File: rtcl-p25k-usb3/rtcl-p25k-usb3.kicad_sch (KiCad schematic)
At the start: 90 parts, among them J1 USB3_B_Micro, J10 SSQ-106-02-F-D-RA, J2 RASPPICAM22, J3 BTB-DF40C-60DS-0.4V(51), J4 BTB-DF40C-60DS-0.4V(51), J5 JTAG, U1 FT601Q, U12 TPS22917DBV, U2 TPD4E05U06DQA, U3 USBLC6-2P6, X1 30MHz

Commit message: Add new footprints for RES_YC104_YAG and RES_YC164_3P2X1P6_YAG
- Created footprint for RES_YC104_YAG with detailed properties and pads.
- Created footprint for RES_YC164_3P2X1P6_YAG with comprehensive design elements and specifications.
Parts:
- removed D1: PTVS5V0Z1USKP, Diode_SMD:Nexperia_DSN1608-2_1.6x0.8mm, symbol Diode:PTVS5V0Z1USKP
- removed L1: BLM18PG221SN1D, Resistor_SMD:R_0402_1005Metric, symbol Device:L
- removed R55: 0, Resistor_SMD:R_0402_1005Metric, symbol Device:R
- added C15: 0.1uF, Capacitor_SMD:C_0603_1608Metric, symbol Device:C
- added FB1: BLM18SG121TN1, symbol Device:FerriteBead
- added R59: 1M, Resistor_SMD:R_0402_1005Metric, symbol Device:R
- added RN2: YC104-JR-0722RL, rtcl-p25k-usb3:RES_YC104_YAG, symbol Device:R_Pack04
- added RN3: YC124-JR-1322RL, rtcl-p25k-usb3:RES_YC164_3P2X1P6_YAG, symbol Device:R_Pack04
- J1: value USB3_B_Micro -> ZX360D-B-10P(30); footprint (none) -> rtcl-p25k-usb3:CONN10_ZX360D-B-10P30_HIR; LCSC (none) -> C598201
- J2: footprint RASPPICAM22 -> (none)
- RN1: value R_Pack04 -> YC164-JR-0722RL; footprint Resistor_SMD:R_Array_Convex_4x0603 -> rtcl-p25k-usb3:RES_YC164_3P2X1P6_YAG
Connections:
- net +5V: now also FB1.2; no longer C10.2, J1.1 (VBUS), U1.37 (VBUS), U3.5 (VBUS)
- net FT601_BE0: now also RN2.4 (R4.1); no longer RN1.5 (R4.2)
- net FT601_BE1: now also RN2.3 (R3.1); no longer RN1.6 (R3.2)
- net FT601_BE2: now also RN2.2 (R2.1); no longer RN1.7 (R2.2)
- net FT601_BE3: now also RN2.1 (R1.1); no longer RN1.8 (R1.2)
- net GND: now also J1.8 (DRAIN), C15.1, R59.2
- net USB_SSRXM: now also U2.4 (D2+); no longer U2.2 (D1-)
- net USB_SSRXP: now also U2.5 (D2-); no longer U2.1 (D1+)
- net USB_SSTXM: now also U2.1 (D1+); no longer U2.5 (D2-)
- net USB_SSTXP: now also U2.2 (D1-); no longer U2.4 (D2+)
- net at J1.SH (SHIELD): now also C15.2, R59.1
- new net VBUS: C10.2, FB1.1, J1.1 (VBUS), U1.37 (VBUS), U3.5 (VBUS)
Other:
- moved on the sheet: RN1

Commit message: WIP
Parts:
- removed R10, R11, R12, R13, R14, R15, R16, R17, R18, R19, R20, R21, R22, R23, R24, R25, R26, R27, R28, R29, R30, R31, R32, R33, R34, R35, R36, R37, R38, R4, R5, R6, R7, R8, R9: 22, Resistor_SMD:R_0402_1005Metric, symbol Device:R

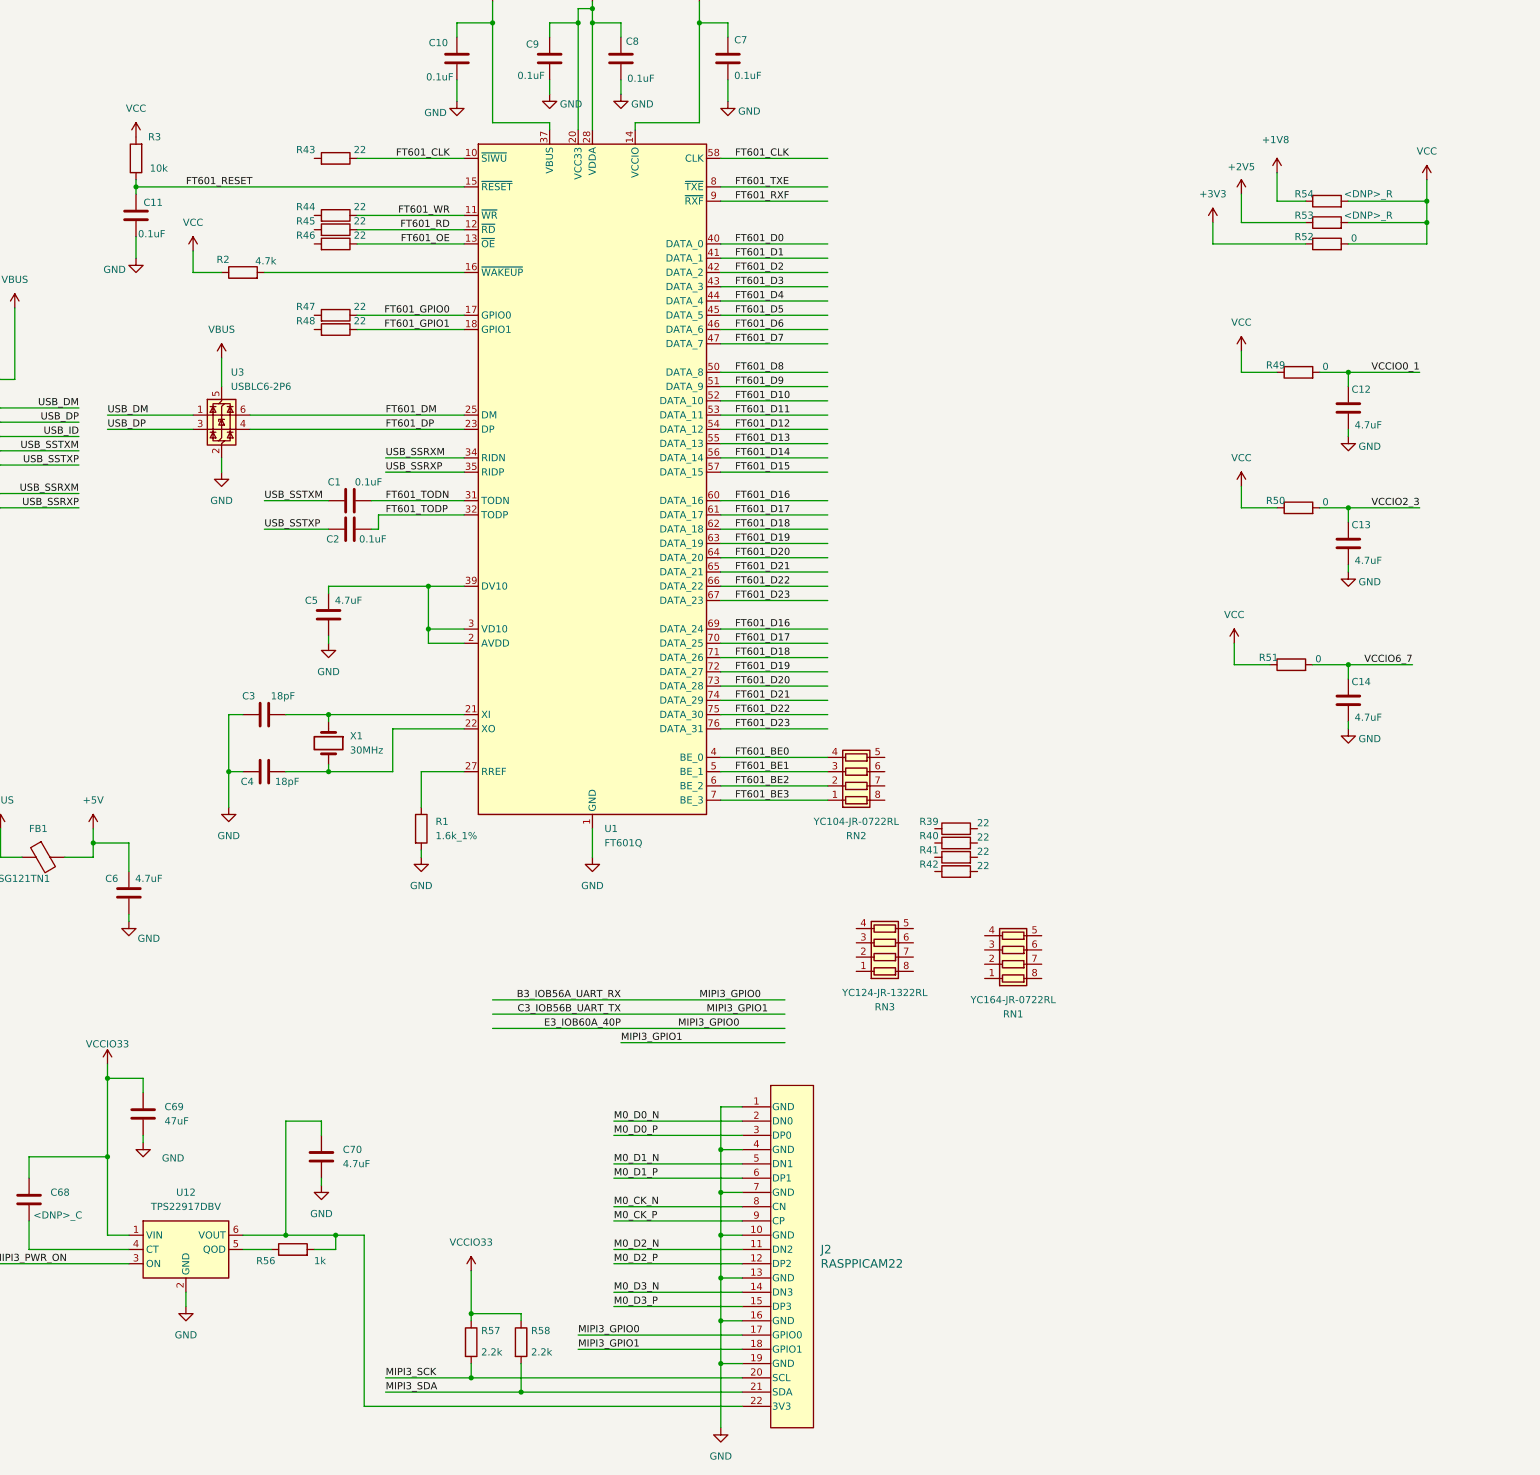
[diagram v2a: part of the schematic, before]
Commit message: Add FT601Q symbol to KiCad library
- Created a new symbol for the FT601Q USB 3.0 FIFO interface IC.
- Included properties such as Reference, Value, Footprint, Datasheet, and Description.
- Defined 77 pins with appropriate names, types, and attributes.
- Ensured compatibility with KiCad version 10.0 and included necessary font settings.
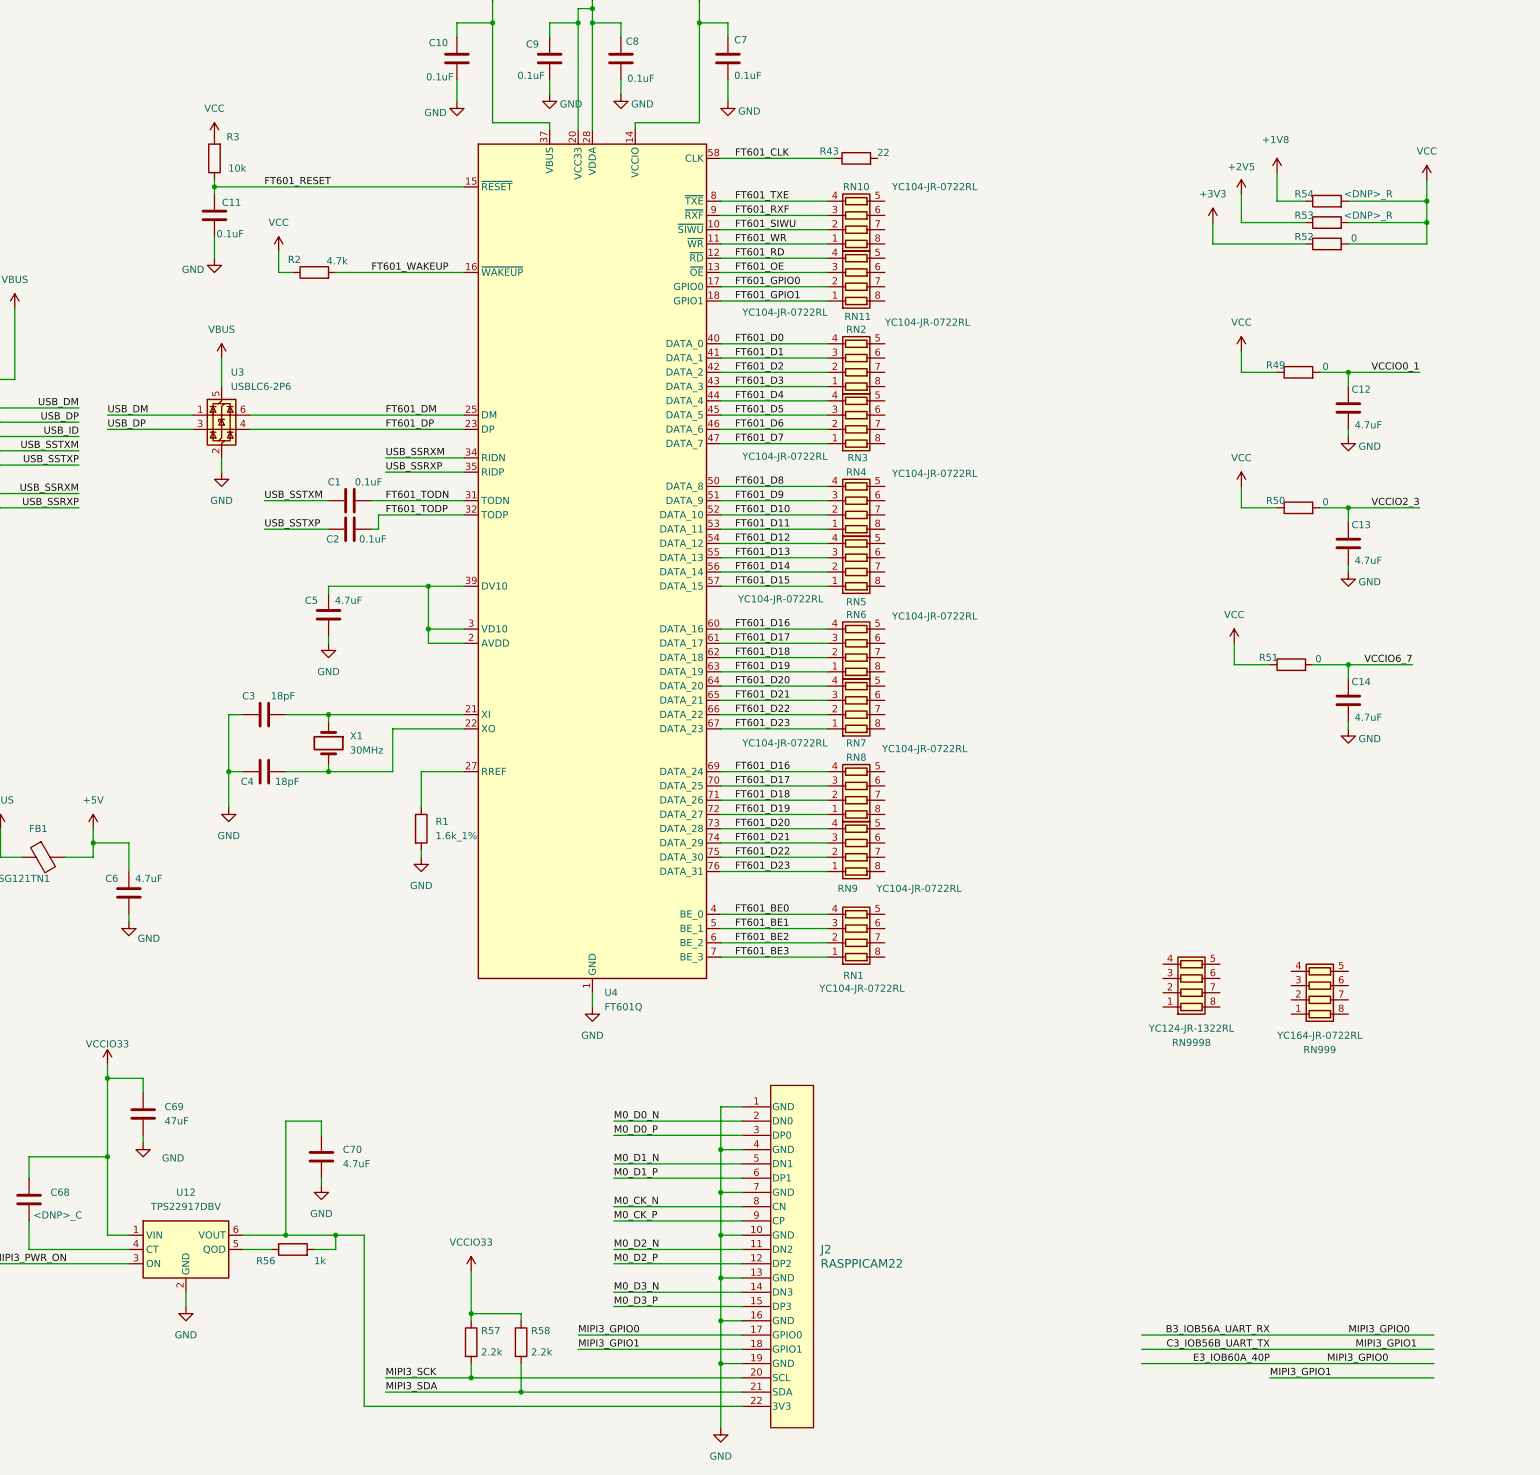
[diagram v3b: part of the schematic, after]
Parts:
- removed R39, R40, R41, R42, R44, R45, R46, R47, R48: 22, Resistor_SMD:R_0402_1005Metric, symbol Device:R
- removed U1: FT601Q, Package_DFN_QFN:QFN-76-1EP_9x9mm_P0.4mm_EP5.81x6.31mm, symbol Interface_USB:FT601Q
- added RN10, RN11, RN2, RN3, RN4, RN5, RN6, RN7, RN8, RN9: YC104-JR-0722RL, rtcl-p25k-usb3:RES_YC104_YAG, symbol Device:R_Pack04
- added U4: FT601Q, Package_DFN_QFN:QFN-76-1EP_9x9mm_P0.4mm_EP5.81x6.31mm, symbol rtcl-p25k-usb3:FT601Q
- renumbered RN2 to RN1, RN1 to RN999, RN3 to RN9998
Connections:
- net +3V3: now also U4.20 (VCC33), U4.24 (VCC33), U4.28 (VDDA), U4.38 (VCC33)
- net FT601_BE0: now also U4.4 (BE_0)
- net FT601_BE1: now also U4.5 (BE_1)
- net FT601_BE2: now also U4.6 (BE_2)
- net FT601_BE3: now also U4.7 (BE_3)
- net FT601_CLK: now also U4.58 (CLK)
- net FT601_D0: now also RN2.4 (R4.1), U4.40 (DATA_0)
- net FT601_D1: now also RN2.3 (R3.1), U4.41 (DATA_1)
- net FT601_D10: now also RN4.2 (R2.1), U4.52 (DATA_10)
- net FT601_D11: now also RN4.1 (R1.1), U4.53 (DATA_11)
- net FT601_D12: now also RN5.4 (R4.1), U4.54 (DATA_12)
- net FT601_D13: now also RN5.3 (R3.1), U4.55 (DATA_13)
- net FT601_D14: now also RN5.2 (R2.1), U4.56 (DATA_14)
- net FT601_D15: now also RN5.1 (R1.1), U4.57 (DATA_15)
- net FT601_D16: now also RN6.4 (R4.1), RN8.4 (R4.1), U4.60 (DATA_16), U4.69 (DATA_24)
- net FT601_D17: now also RN6.3 (R3.1), RN8.3 (R3.1), U4.61 (DATA_17), U4.70 (DATA_25)
- net FT601_D18: now also RN6.2 (R2.1), RN8.2 (R2.1), U4.62 (DATA_18), U4.71 (DATA_26)
- net FT601_D19: now also RN6.1 (R1.1), RN8.1 (R1.1), U4.63 (DATA_19), U4.72 (DATA_27)
- net FT601_D2: now also RN2.2 (R2.1), U4.42 (DATA_2)
- net FT601_D20: now also RN7.4 (R4.1), RN9.4 (R4.1), U4.64 (DATA_20), U4.73 (DATA_28)
- net FT601_D21: now also RN7.3 (R3.1), RN9.3 (R3.1), U4.65 (DATA_21), U4.74 (DATA_29)
- net FT601_D22: now also RN7.2 (R2.1), RN9.2 (R2.1), U4.66 (DATA_22), U4.75 (DATA_30)
- net FT601_D23: now also RN7.1 (R1.1), RN9.1 (R1.1), U4.67 (DATA_23), U4.76 (DATA_31)
- net FT601_D3: now also RN2.1 (R1.1), U4.43 (DATA_3)
- net FT601_D4: now also RN3.4 (R4.1), U4.44 (DATA_4)
- net FT601_D5: now also RN3.3 (R3.1), U4.45 (DATA_5)
- net FT601_D6: now also RN3.2 (R2.1), U4.46 (DATA_6)
- net FT601_D7: now also RN3.1 (R1.1), U4.47 (DATA_7)
- net FT601_D8: now also RN4.4 (R4.1), U4.50 (DATA_8)
- net FT601_D9: now also RN4.3 (R3.1), U4.51 (DATA_9)
- net FT601_DM: now also U4.25 (DM)
- net FT601_DP: now also U4.23 (DP)
- net FT601_GPIO0: now also RN11.2 (R2.1), U4.17 (GPIO0)
- net FT601_GPIO1: now also RN11.1 (R1.1), U4.18 (GPIO1)
- net FT601_OE: now also RN11.3 (R3.1), U4.13 (~{OE})
- net FT601_RD: now also RN11.4 (R4.1), U4.12 (~{RD})
- net FT601_RESET: now also U4.15 (~{RESET})
- net FT601_RXF: now also RN10.3 (R3.1), U4.9 (~{RXF})
- net FT601_TODN: now also U4.31 (TODN)
- net FT601_TODP: now also U4.32 (TODP)
- net FT601_TXE: now also RN10.4 (R4.1), U4.8 (~{TXE})
- net FT601_WR: now also RN10.1 (R1.1), U4.11 (~{WR})
- net GND: now also U4.1 (GND), U4.26 (GND), U4.29 (GND), U4.36 (GND), U4.77 (GND)
- net USB_SSRXM: now also U4.34 (RIDN)
- net USB_SSRXP: now also U4.35 (RIDP)
- net VBUS: now also U4.37 (VBUS)
- net VCC: now also U4.14 (VCCIO), U4.49 (VCCIO), U4.59 (VCCIO), U4.68 (VCCIO)
- net at C3.2, X1.1: now also U4.21 (XI)
- net at R1.1: now also U4.27 (RREF)
- net FT601_WAKEUP: now reaches R2.2
- net FT601_WAKEUP: now also U4.16 (~{WAKEUP})
- net at C5.2: now also U4.2 (AVDD), U4.3 (VD10), U4.30 (VD10), U4.33 (VD10), U4.39 (DV10), U4.48 (VD10)
- net at C4.2, X1.2: now also U4.22 (XO)
- new net FT601_SIWU: RN10.2 (R2.1), U4.10 (~{SIWU})
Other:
- moved on the sheet: C11, R2, R3, RN1, RN999, RN9998

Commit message: WIP
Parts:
- J2: value RASPPICAM22 -> 0525592253
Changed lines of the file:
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@@
 			)
 		)
-		(property "Value" "RASPPICAM22"
+		(property "Value" "0525592253"
 			(at 186.69 356.8699 0)
 			(show_name no)

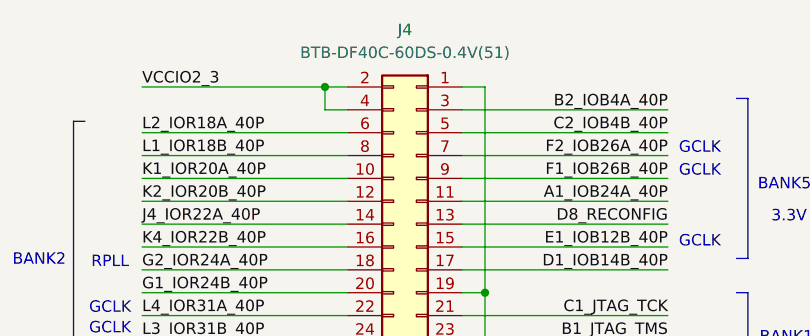
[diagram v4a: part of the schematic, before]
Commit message: Update KiCad project files for rtcl-p25k-usb3
- Changed active layer from 25 to 5 in the project file.
- Updated footprint property for components in the schematic:
  - Changed footprint for a connector to "rtcl-p25k-usb3:CON_525592253_MOL".
  - Updated value for a component from "BTB-DF40C-60DS-0.4V(51)" to "DF40C-60DS-0.4V(51)".
  - Changed footprint for another component to "rtcl-p25k-usb3:PMOD_02x06_2.54mm".
- Modified UUIDs for various graphical elements in the CONN_DF40C-60DS_HIR module.
- Added a 3D model reference for the DF40C-60DS-0.4V(51) component.
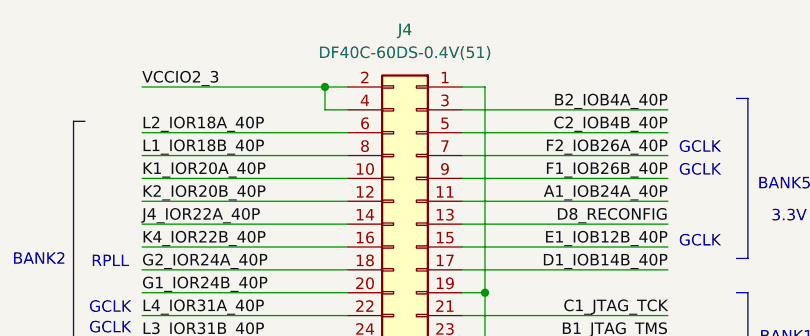
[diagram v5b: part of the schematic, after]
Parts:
- J10: footprint mipi_spartan7:PH_02x06_2.54mm -> rtcl-p25k-usb3:PMOD_02x06_2.54mm
- J2: footprint (none) -> rtcl-p25k-usb3:CON_525592253_MOL
- J4: value BTB-DF40C-60DS-0.4V(51) -> DF40C-60DS-0.4V(51)
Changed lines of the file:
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@@
 			)
 		)
-		(property "Footprint" ""
+		(property "Footprint" "rtcl-p25k-usb3:CON_525592253_MOL"
 			(at 181.864 315.722 0)
 			(hide yes)
@@
 			)
 		)
-		(property "Value" "BTB-DF40C-60DS-0.4V(51)"
+		(property "Value" "DF40C-60DS-0.4V(51)"
 			(at 350.52 31.75 0)
 			(show_name no)
@@
 			)
 		)
-		(property "Footprint" "mipi_spartan7:PH_02x06_2.54mm"
+		(property "Footprint" "rtcl-p25k-usb3:PMOD_02x06_2.54mm"
 			(at 406.4 203.2 0)
 			(hide yes)

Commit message: WIP
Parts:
- added C16, C17, C18, C19, C20: 0.1uF, Capacitor_SMD:C_0402_1005Metric, symbol Device:C
- J5: footprint Connector_PinHeader_2.54mm:PinHeader_1x08_P2.54mm_Vertical -> Connector_PinHeader_2.54mm:PinHeader_1x06_P2.54mm_Vertical
- renumbered U4 to U1
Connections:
- net +3V3: now also C19.2, C20.2
- net GND: now also C16.1, C17.1, C18.1, C19.1, C20.1
- net VCC: now also C16.2, C17.2, C18.2
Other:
- moved on the sheet: C10, C7, C8, C9, R43, RN1, RN10, RN11, RN2, RN3, RN4, RN5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

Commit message: Refactor code structure for improved readability and maintainability
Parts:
- removed RN10, RN11: YC104-JR-0722RL, rtcl-p25k-usb3:RES_YC104_YAG, symbol Device:R_Pack04
- added R44, R45, R46, R47: 22, Resistor_SMD:R_0402_1005Metric, symbol Device:R
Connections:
- net B3_IOB56A_UART_RX: no longer J2.17 (GPIO0), J3.23 (Pin_23)
- net C3_IOB56B_UART_TX: no longer J2.18 (GPIO1)
- net FT601_GPIO0: now also R46.1
- net FT601_GPIO1: now also R47.1
- net FT601_RXF: now also R45.1
- net FT601_TXE: now also R44.1
- net MIPI3_SDA: no longer J2.21 (SDA), R58.2
- net G7_IOT68B renamed G8_IOT68B
- net MIPI3_SCK renamed MIPI_SCL
- new net E3_IOB60A_40P: J3.23 (Pin_23)
- new net MIPI_GPIO0: J2.17 (GPIO0)
- new net MIPI_GPIO1: J2.18 (GPIO1)
- new net MIPI_SDA: J2.21 (SDA), R58.2
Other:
- moved on the sheet: C1, C10, C11, C12, C13, C14, C15, C16, C17, C18, C19, C2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
